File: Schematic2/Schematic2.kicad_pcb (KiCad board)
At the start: 2 copper layers, 43 parts, among them U1 Kailhlowprofile, U10 Kailhlowprofile, U11 Kailhlowprofile, U12 Kailhlowprofile, U13 Kailhlowprofile, U14 Kailhlowprofile, U15 Kailhlowprofile, U16 Kailhlowprofile, U17 Kailhlowprofile, U18 Kailhlowprofile, U19 Kailhlowprofile, U2 Kailhlowprofile, U20 Kailhlowprofile, U21 Kailhlowprofile, U3 Kailhlowprofile, U4 Kailhlowprofile, U5 Kailhlowprofile, U6 Kailhlowprofile, U7 Kailhlowprofile, U8 Kailhlowprofile, U9 Kailhlowprofile

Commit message: Schematic3
19/03/2019 23:59
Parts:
- removed D21: 1N4148, 1N4148:DIOAD829W49L456D191
- removed U21: Kailhlowprofile, keyswitches:Kailh_socket_optional_reversible
- PCB2: value VAL** -> ARDUINO_MICRO
- U1, U10, U11, U12, U13, U14, U15, U16, U17, U18, U19, U2, U20, U3, U4, U5, U6, U7, U8, U9: footprint keyswitches:Kailh_socket_optional_reversible -> Keebio-Parts:Kailh-PG1350-1u-No-Clickhole
- moved PCB2 248.4 mm to (272.7, 63.9), turned to 180 degrees
- moved U16 228.8 mm to (262.4, 115.0)
- moved U20 226.6 mm to (262.9, 138.4)
- moved D20 221.9 mm to (266.7, 149.9), turned to 180 degrees
- moved U19 217.0 mm to (241.3, 138.4)
- moved D19 201.2 mm to (245.1, 149.9), turned to 180 degrees
- moved U2 184.9 mm to (220.4, 55.0)
- moved U11 171.5 mm to (241.4, 95.0)
- moved D18 166.7 mm to (224.8, 149.9), turned to 180 degrees
- moved U17 161.9 mm to (199.4, 138.4)
- moved U18 161.4 mm to (221.0, 138.4)
- moved U15 160.1 mm to (241.4, 115.0)
- moved D16 159.7 mm to (266.6, 124.8), turned to 180 degrees
- moved U14 157.7 mm to (220.4, 115.0)
- moved D11 154.8 mm to (245.6, 105.0), turned to 180 degrees
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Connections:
- D1 pad C: Net-(D1-PadC) -> R2
- D10 pad C: Net-(D10-PadC) -> R5
- D11 pad C: Net-(D1-PadC) -> R2
- D12 pad C: Net-(D12-PadC) -> R1
- D13 pad C: Net-(D13-PadC) -> R3
- D14 pad C: Net-(D14-PadC) -> R4
- D15 pad C: Net-(D10-PadC) -> R5
- D16 pad C: Net-(D1-PadC) -> R2
- D17 pad C: Net-(D12-PadC) -> R1
- D18 pad C: Net-(D13-PadC) -> R3
- D19 pad C: Net-(D14-PadC) -> R4
- D2 pad C: Net-(D12-PadC) -> R1
- D20 pad C: Net-(D10-PadC) -> R5
- D3 pad C: Net-(D13-PadC) -> R3
- D4 pad C: Net-(D14-PadC) -> R4
- D5 pad C: Net-(D10-PadC) -> R5
- D6 pad C: Net-(D1-PadC) -> R2
- D7 pad C: Net-(D12-PadC) -> R1
- D8 pad C: Net-(D13-PadC) -> R3
- D9 pad C: Net-(D14-PadC) -> R4
- PCB2 pad D13: Net-(D12-PadC) -> Net-(PCB2-PadD13)
- PCB2 pad GND.: Net-(PCB2-PadGND.) -> R2
- PCB2 pad MISO]: Net-(PCB2-PadMISO]) -> R4
- PCB2 pad RST.: Net-(PCB2-PadRST.) -> R1
- PCB2 pad SCK: Net-(PCB2-PadSCK) -> R5
- PCB2 pad VIN: Net-(PCB2-PadVIN) -> R3
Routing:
- net R2: track 0.00 -> 29.6 mm
- net Net-(D3-PadA): track 0.00 -> 4.62 mm
- net Net-(D4-PadA): track 0.00 -> 4.61 mm
- net Net-(D2-PadA): track 0.00 -> 4.61 mm
- net Net-(D1-PadA): track 0.00 -> 4.48 mm
- net Net-(D7-PadA): track 0.00 -> 4.47 mm
- net Net-(D5-PadA): track 0.00 -> 4.46 mm
- net Net-(D11-PadA): track 0.00 -> 4.46 mm
- net Net-(D6-PadA): track 0.00 -> 4.44 mm
- net Net-(D13-PadA): track 0.00 -> 4.42 mm
- net Net-(D10-PadA): track 0.00 -> 4.42 mm
- net Net-(D15-PadA): track 0.00 -> 4.42 mm
- net Net-(D9-PadA): track 0.00 -> 4.41 mm
- net Net-(D8-PadA): track 0.00 -> 4.41 mm
- net Net-(D14-PadA): track 0.00 -> 4.40 mm
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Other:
- board outline added: 104.9 x 101.4 mm

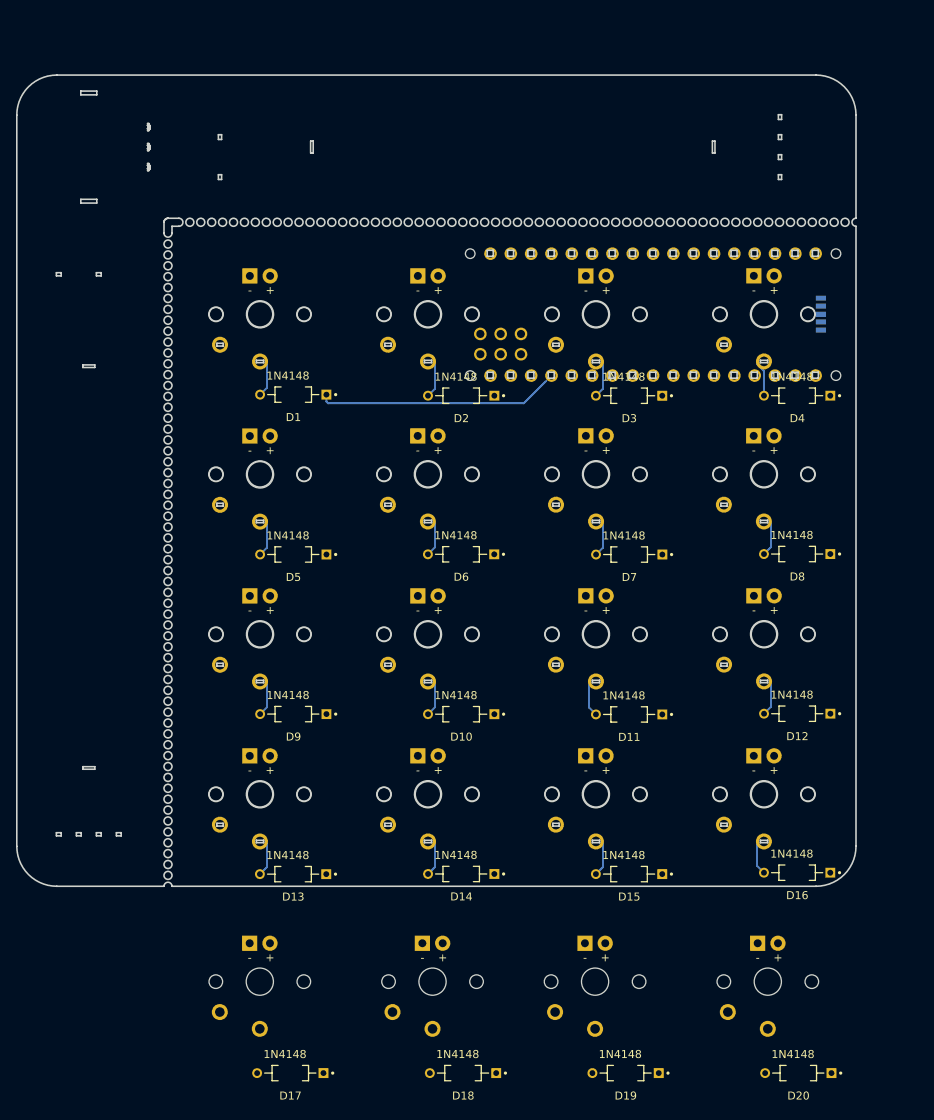
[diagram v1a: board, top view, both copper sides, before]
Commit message: Finalized keyboard schem
Circuit finished
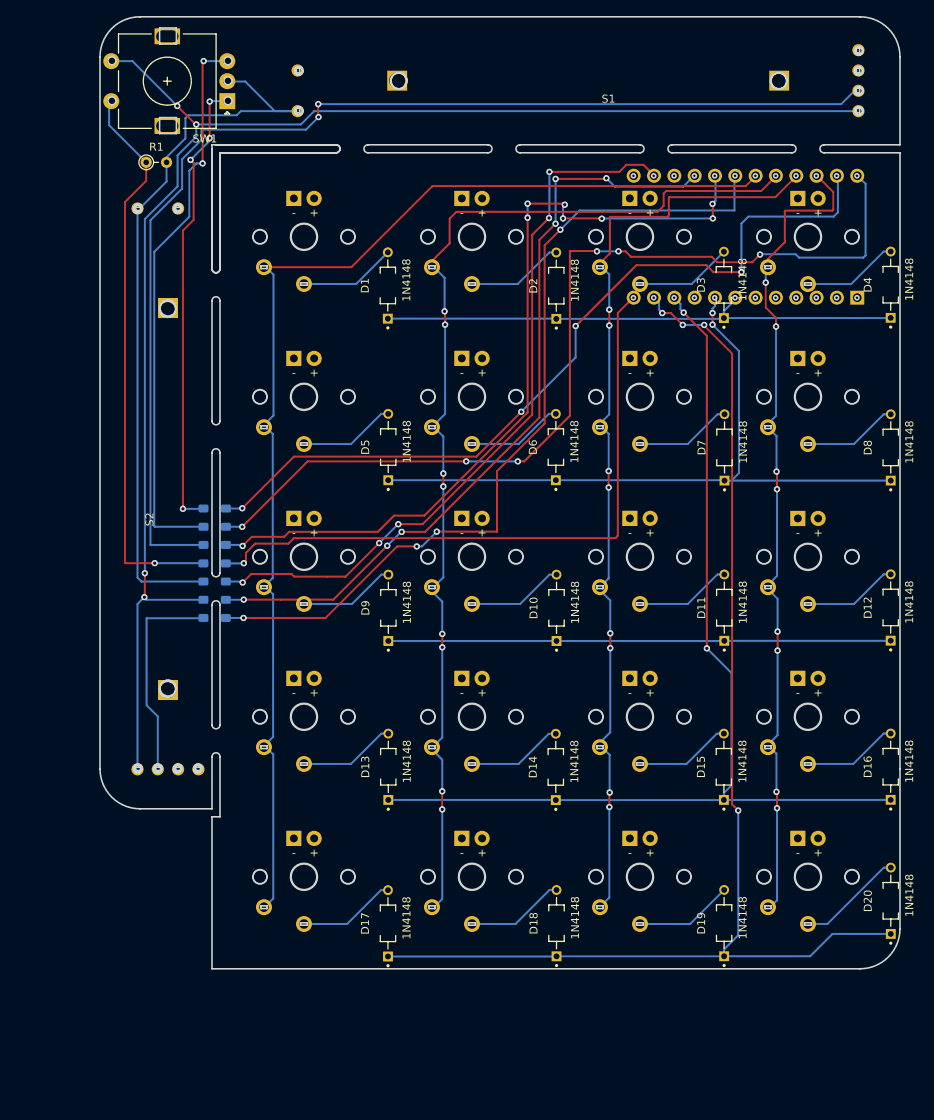
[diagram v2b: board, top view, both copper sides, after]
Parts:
- removed PCB2: ARDUINO_MICRO, ARDUINO_MICRO:ARDUINO_MICRO
- added Ard1: ProMicro, keebs:Pro_Micro, B.Cu at (260.1, 45.3)
- added R1: R, Resistor_THT:R_Axial_DIN0204_L3.6mm_D1.6mm_P2.54mm_Vertical, F.Cu at (185.2, 36.0)
- added REF**: C_1206_3216MetricBRYGGA, Capacitor_SMD:C_1206_3216MetricBRYGGA, B.Cu at (193.7, 93.0)
- added REF**: C_1206_3216MetricBRYGGA, Capacitor_SMD:C_1206_3216MetricBRYGGA, B.Cu at (193.8, 83.8)
- added REF**: C_1206_3216MetricBRYGGA, Capacitor_SMD:C_1206_3216MetricBRYGGA, B.Cu at (193.7, 86.2)
- added REF**: C_1206_3216MetricBRYGGA, Capacitor_SMD:C_1206_3216MetricBRYGGA, B.Cu at (193.7, 90.7)
- added REF**: C_1206_3216MetricBRYGGA, Capacitor_SMD:C_1206_3216MetricBRYGGA, B.Cu at (193.8, 81.6)
- added REF**: C_1206_3216MetricBRYGGA, Capacitor_SMD:C_1206_3216MetricBRYGGA, B.Cu at (193.7, 88.4)
- added REF**: C_1206_3216MetricBRYGGA, Capacitor_SMD:C_1206_3216MetricBRYGGA, B.Cu at (193.8, 79.3)
- added S1: Slider_ALPS, alps_slider:ALPS-Slider, F.Cu at (236.1, 25.8)
- added S2: Slider_ALPS, alps_slider:ALPS-Slider, F.Cu at (187.9, 73.8)
- added SW1: Rotary_Encoder_Switch, Rotary_Encoder:RotaryEncoder_Alps_EC11E-Switch_Vertical_H20mm, F.Cu at (195.3, 28.4)
- moved D20 24.4 mm to (278.3, 128.3), turned to 90 degrees
- moved D19 22.4 mm to (257.4, 131.1), turned to 90 degrees
- moved D17 22.4 mm to (215.4, 131.1), turned to 90 degrees
- moved D18 22.1 mm to (236.5, 131.1), turned to 90 degrees
- moved D3 18.2 mm to (257.4, 51.3), turned to 90 degrees
- moved D2 18.2 mm to (236.4, 51.4), turned to 90 degrees
- moved D4 18.1 mm to (278.2, 51.3), turned to 90 degrees
- moved D1 18.1 mm to (215.4, 51.4), turned to 90 degrees
- moved D13 17.9 mm to (215.4, 111.6), turned to 90 degrees
- moved D5 17.9 mm to (215.4, 71.6), turned to 90 degrees
- moved D7 17.9 mm to (257.5, 71.7), turned to 90 degrees
- moved D15 17.9 mm to (257.4, 111.6), turned to 90 degrees
- moved D6 17.9 mm to (236.4, 71.6), turned to 90 degrees
- moved D11 17.9 mm to (257.4, 91.7), turned to 90 degrees
- moved D14 17.9 mm to (236.4, 111.6), turned to 90 degrees
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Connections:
- D1 pad C: R2 -> R1
- D10 pad C: R5 -> R3
- D11 pad C: R2 -> R3
- D12 pad C: R1 -> R3
- D13 pad C: R3 -> R4
- D15 pad C: R5 -> R4
- D16 pad C: R2 -> R4
- D17 pad C: R1 -> R5
- D18 pad C: R3 -> R5
- D19 pad C: R4 -> R5
- D3 pad C: R3 -> R1
- D4 pad C: R4 -> R1
- D5 pad C: R5 -> R2
- D7 pad C: R1 -> R2
- D8 pad C: R3 -> R2
- D9 pad C: R4 -> R3
- U12 pad 2: C3 -> C4
- U13 pad 2: C3 -> C1
- U14 pad 2: C3 -> C2
- U17 pad 2: C4 -> C1
- U18 pad 2: C4 -> C2
- U19 pad 2: C4 -> C3
- U2 pad 2: C1 -> C2
- U3 pad 2: C1 -> C3
- U4 pad 2: C1 -> C4
- U7 pad 2: C2 -> C3
- U8 pad 2: C2 -> C4
- U9 pad 2: C2 -> C1
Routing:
- net (no net): track 0.00 -> 759.8 mm, vias 0 -> 40
- net S1: track 0.00 -> 198.9 mm, vias 0 -> 4
- net R5: track 0.00 -> 153.0 mm, vias 0 -> 4
- net C1: track 0.00 -> 151.2 mm
- net S2: track 0.00 -> 149.8 mm, vias 0 -> 2
- net C2: track 0.00 -> 137.0 mm, vias 0 -> 8
- net R4: track 0.00 -> 128.3 mm, vias 0 -> 2
- net C3: track 0.00 -> 118.6 mm, vias 0 -> 8
- net C4: track 0.00 -> 103.7 mm, vias 0 -> 8
- net SwEn2: track 0.00 -> 100.1 mm, vias 0 -> 1
- net S2-3: track 0.00 -> 97.4 mm
- net R1: track 0.00 -> 65.3 mm
- net R3: track 0.00 -> 62.8 mm
- net R2: track 29.6 -> 86.9 mm, vias 0 -> 2
- net S2-2: track 0.00 -> 30.9 mm
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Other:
- board size 104.9 x 101.4 mm -> 100 x 119 mm
- board text added: "GND"
- board text added: "Pin12"
- board text added: "Pin13"
- board text added: "Pin14"
- board text added: "Pin19"
- board text added: "Pin20"
- board text added: "VCC"

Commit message: THE FINAL
urgh. Last and final PCB
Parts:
- moved S1 0.50 mm to (235.6, 25.8)
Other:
- outline, holes or cut-outs redrawn
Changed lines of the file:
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@@
   )
   (module alps_slider:ALPS-Slider (layer F.Cu)
-    (at 236.1184 25.8064 180)
+    (at 235.6184 25.8064 180)
     (fp_text reference S1 (at -6.858 -2.286 180) (layer F.SilkS)
       (effects (font (size 1 1) (thickness 0.15)))
@@
   (gr_line (start 242.311999 89.299) (end 241.511999 89.299) (layer Edge.Cuts) (width 0.2))
   (gr_circle (center 252.411999 105.324) (end 253.312 105.324) (layer Edge.Cuts) (width 0.2))
-  (gr_circle (center 204.302975 24.573999) (end 204.802975 24.573999) (layer Edge.Cuts) (width 0.2))
+  (gr_circle (center 203.702975 24.573999) (end 204.202975 24.573999) (layer Edge.Cuts) (width 0.2))
   (gr_line (start 194.411999 110.324) (end 194.411999 117.824) (layer Edge.Cuts) (width 0.2))
   (gr_arc (start 193.911999 110.324) (end 194.411999 110.324) (angle -180) (layer Edge.Cuts) (width 0.2))
@@
   (gr_line (start 193.412 91.324) (end 193.412 106.324) (layer Edge.Cuts) (width 0.2))
   (gr_line (start 188.962 32.423999) (end 186.862 32.423999) (layer Edge.Cuts) (width 0.2))
-  (gr_circle (center 274.302975 27.073999) (end 274.802975 27.073999) (layer Edge.Cuts) (width 0.2))
+  (gr_circle (center 273.702975 27.073999) (end 274.202975 27.073999) (layer Edge.Cuts) (width 0.2))
   (gr_circle (center 186.662 111.723999) (end 187.162 111.723999) (layer Edge.Cuts) (width 0.2))
   (gr_circle (center 195.411999 25.823999) (end 195.911999 25.823999) (layer Edge.Cuts) (width 0.2))
-  (gr_circle (center 204.302975 29.573999) (end 204.802975 29.573999) (layer Edge.Cuts) (width 0.2))
-  (gr_circle (center 264.302975 25.814975) (end 265.302975 25.814975) (layer Edge.Cuts) (width 0.2))
+  (gr_circle (center 203.702975 29.573999) (end 204.202975 29.573999) (layer Edge.Cuts) (width 0.2))
+  (gr_circle (center 263.702975 25.814975) (end 264.702975 25.814975) (layer Edge.Cuts) (width 0.2))
   (gr_line (start 186.862 32.423999) (end 186.862 30.423999) (layer Edge.Cuts) (width 0.2))
   (gr_line (start 186.862 30.423999) (end 188.962 30.423999) (layer Edge.Cuts) (width 0.2))
@@
   (gr_line (start 194.411999 72.324) (end 194.411999 87.324) (layer Edge.Cuts) (width 0.2))
   (gr_arc (start 193.911999 106.324) (end 193.412 106.324) (angle -180) (layer Edge.Cuts) (width 0.2))
-  (gr_circle (center 274.302975 24.573999) (end 274.802975 24.573999) (layer Edge.Cuts) (width 0.2))
+  (gr_circle (center 273.702975 24.573999) (end 274.202975 24.573999) (layer Edge.Cuts) (width 0.2))
   (gr_circle (center 180.912 23.323999) (end 181.412 23.323999) (layer Edge.Cuts) (width 0.2))
   (gr_circle (center 189.162 111.723999) (end 189.662 111.723999) (layer Edge.Cuts) (width 0.2))
-  (gr_circle (center 216.802975 25.814975) (end 217.802975 25.814975) (layer Edge.Cuts) (width 0.2))
+  (gr_circle (center 216.202975 25.814975) (end 217.202975 25.814975) (layer Edge.Cuts) (width 0.2))
   (gr_arc (start 274.412 131.823999) (end 274.412 136.823999) (angle -90) (layer Edge.Cuts) (width 0.2))
   (gr_line (start 279.412 111.824) (end 279.412 131.823999) (layer Edge.Cuts) (width 0.2))
@@
   (gr_line (start 179.412 22.823999) (end 179.412 111.823999) (layer Edge.Cuts) (width 0.2))
   (gr_circle (center 195.411999 28.323999) (end 195.911999 28.323999) (layer Edge.Cuts) (width 0.2))
-  (gr_circle (center 274.302975 29.573999) (end 274.802975 29.573999) (layer Edge.Cuts) (width 0.2))
+  (gr_circle (center 273.702975 29.573999) (end 274.202975 29.573999) (layer Edge.Cuts) (width 0.2))
   (gr_circle (center 184.162 41.723999) (end 184.662 41.723999) (layer Edge.Cuts) (width 0.2))
-  (gr_circle (center 274.302975 22.073999) (end 274.802975 22.073999) (layer Edge.Cuts) (width 0.2))
+  (gr_circle (center 273.702975 22.073999) (end 274.202975 22.073999) (layer Edge.Cuts) (width 0.2))
   (gr_circle (center 262.411999 65.324) (end 263.311999 65.324) (layer Edge.Cuts) (width 0.2))
   (gr_circle (center 262.411999 85.324) (end 263.311999 85.324) (layer Edge.Cuts) (width 0.2))
